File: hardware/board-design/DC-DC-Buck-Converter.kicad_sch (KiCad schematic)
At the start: 18 parts, among them U1 Gate Driver

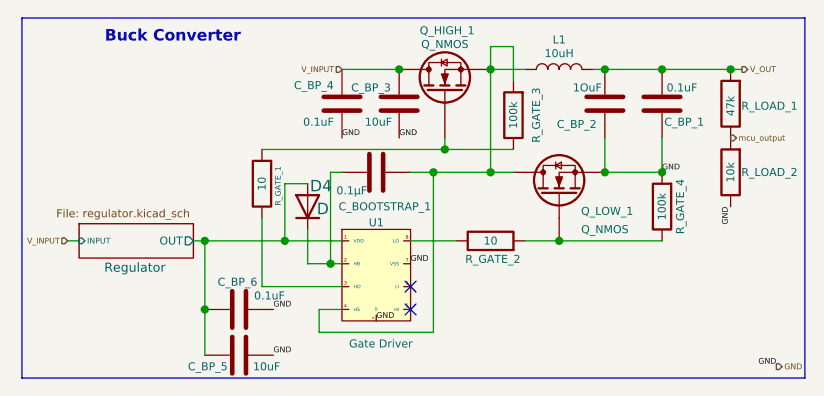
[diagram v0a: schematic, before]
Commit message: feat(schematic): redesign buck converter circuit
Replaced the gate driver and regulator stage with a dedicated Buck Controller IC to resolve missing feedback loops and completed the schematic redesign.
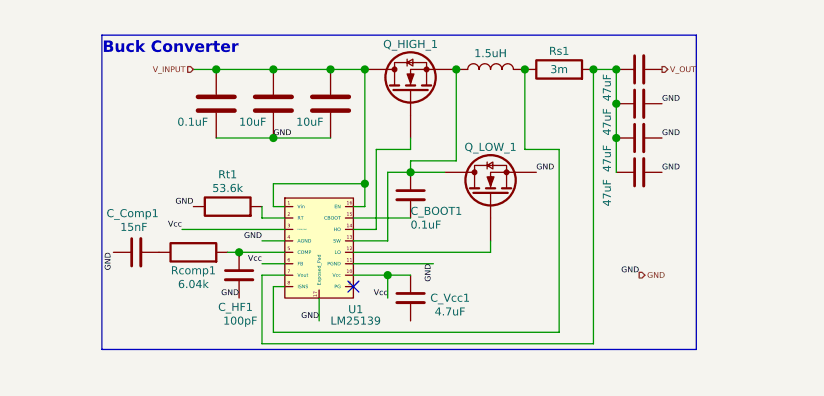
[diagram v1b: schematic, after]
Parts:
- removed C_BOOTSTRAP_1: 0.1µF, Capacitor_SMD:C_0603_1608Metric_Pad1.08x0.95mm_HandSolder, symbol Device:C
- removed C_BP_1, C_BP_6: 0.1uF, Capacitor_SMD:C_0603_1608Metric_Pad1.08x0.95mm_HandSolder, symbol Device:C
- removed C_BP_2: 1OuF, Custom-lib:CAPC6153X390N, symbol Device:C
- removed D4: D, symbol Device:D
- removed R_GATE_1, R_GATE_2: 10, Resistor_SMD:R_0603_1608Metric_Pad0.98x0.95mm_HandSolder, symbol Device:R
- removed R_GATE_3, R_GATE_4: 100k, Resistor_SMD:R_0402_1005Metric_Pad0.72x0.64mm_HandSolder, symbol Device:R
- removed R_LOAD_1: 47k, Resistor_SMD:R_0603_1608Metric_Pad0.98x0.95mm_HandSolder, symbol Device:R
- removed R_LOAD_2: 10k, Resistor_SMD:R_0402_1005Metric_Pad0.72x0.64mm_HandSolder, symbol Device:R
- removed U1: Gate Driver, Custom-lib:SON8 (DRM) (4 mm × 4 mm), symbol Driver_FET:Custom-GateDRVR
- added C_BOOT1: 0.1uF, symbol Device:C_Small
- added C_Comp1: 15nF, symbol Device:C_Small
- added C_HF1: 100pF, symbol Device:C_Small
- added C_Vcc1: 4.7uF, symbol Device:C_Small
- added C_out1, C_out2, C_out3, C_out4: 47uF, symbol Device:C_Small
- added Rcomp1: 6.04k, symbol Device:R
- added Rs1: 3m, symbol Device:R
- added Rt1: 53.6k, symbol Device:R
- added U1: LM25139, Package_DFN_QFN:VQFN-16-1EP_3x3mm_P0.5mm_EP1.68x1.68mm, symbol MySymbols:LM25139
- L1: value 10uH -> 1.5uH
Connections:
- net Regulator/OUT is gone; now on net V_INPUT: C_BP_5.1
- net GND: now also C_Comp1.1, C_HF1.2, C_out1.2, C_out2.2, C_out3.2, Rt1.1, U1.11 (PGND), U1.17 (Exposed_Pad), U1.4 (AGND)
- net V_INPUT: now also U1.1 (Vin), U1.16 (EN)
- net V_OUT: now also C_out4.2; no longer L1.2
- net at L1.1, Q_HIGH_1.S, Q_LOW_1.D: now also C_BOOT1.1, U1.13 (SW)
- net at Q_LOW_1.G: now also U1.12 (LO)
- net at Q_HIGH_1.G: now also U1.14 (HO)
- new net: C_Comp1.2, Rcomp1.1
- new net: C_out1.1, C_out2.1, C_out3.1, C_out4.1, Rs1.2, U1.7 (Vout)
- new net: L1.2, Rs1.1, U1.8 (ISNS)
- new net: C_BOOT1.2, U1.15 (CBOOT)
- new net: Rt1.2, U1.2 (RT)
- new net: C_HF1.1, Rcomp1.2, U1.5 (COMP)
- new net Vcc: C_Vcc1.1, U1.10 (Vcc), U1.3 (FPWM/SYNC), U1.6 (FB)
- no-connect marks 2 -> 1
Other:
- removed sheet Regulator
- moved on the sheet: Q_HIGH_1, Q_LOW_1

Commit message: feat(component-properties): complate properties
Add datasheets, footprints, part numbers and manufacterer names
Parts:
- C_BOOT1: footprint (none) -> Capacitor_SMD:C_0603_1608Metric_Pad1.08x0.95mm_HandSolder; Manufacturer (none) -> Murata Electronics; PART NUMBER (none) -> GRM188R72A104KA35D
- C_BP_3, C_BP_4, C_BP_5: Manufacturer Murata -> Murata Electronics
- C_Comp1: footprint (none) -> Capacitor_SMD:C_0603_1608Metric_Pad1.08x0.95mm_HandSolder; Manufacturer (none) -> Murata Electronics; PART NUMBER (none) -> GCM188R72A153KA37D
- C_HF1: footprint (none) -> Capacitor_SMD:C_0603_1608Metric_Pad1.08x0.95mm_HandSolder; Manufacturer (none) -> Murata Electronics; PART NUMBER (none) -> GRM1885C1H101JA01D
- C_Vcc1: footprint (none) -> Capacitor_SMD:C_0805_2012Metric_Pad1.18x1.45mm_HandSolder; Manufacturer (none) -> Murata Electronics; PART NUMBER (none) -> GRM21BZ71H475KE15L
- C_out1, C_out2, C_out3, C_out4: footprint (none) -> Custom-lib:CAPC6075X690N; Manufacturer (none) -> TDK; PART NUMBER (none) -> CAA573X7S2A476M640LH
- L1: footprint Custom-lib:WE-HCI_2212 -> Custom-lib:WE-LHMI_7030; PART NUMBER 74435581000 -> 74437346015
- Rcomp1: footprint (none) -> Resistor_SMD:R_0603_1608Metric_Pad0.98x0.95mm_HandSolder; Manufacturer (none) -> Vishay; PART NUMBER (none) -> CRCW06036K04FKEA
- Rs1: footprint (none) -> Resistor_SMD:R_0612_1632Metric_Pad1.18x3.40mm_HandSolder; Manufacturer (none) -> Vishay; PART NUMBER (none) -> WSKW06123L000FEA
- Rt1: footprint (none) -> Resistor_SMD:R_0603_1608Metric_Pad0.98x0.95mm_HandSolder; Manufacturer (none) -> Vishay; PART NUMBER (none) -> CRCW060353K6FKEA
- U1: PART NUMBER (none) -> LM25139RGTR; Part Number LM25139RGTR -> (none)
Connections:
- net GND: now also C_Vcc1.2

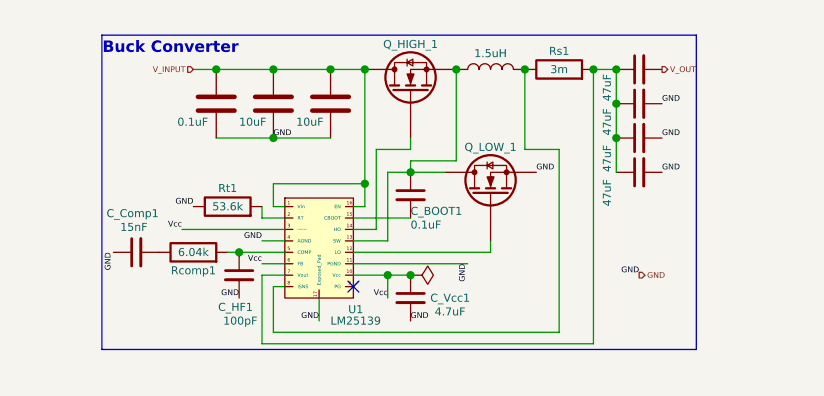
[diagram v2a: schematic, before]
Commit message: feat(schematic): add new symbol and footprint
add for High-MOS and Low-MOS.
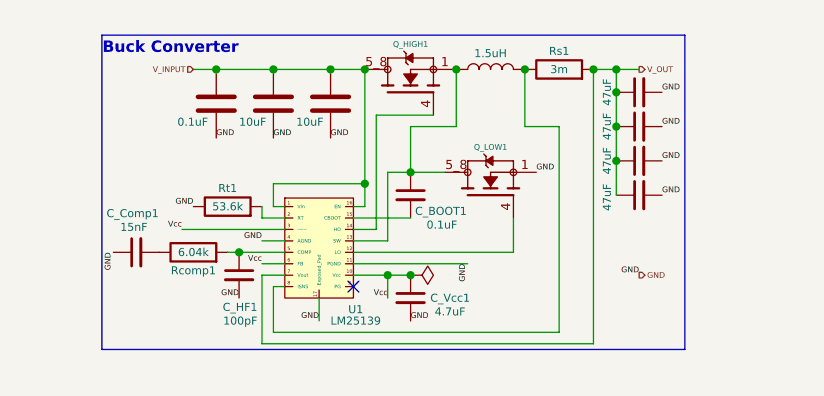
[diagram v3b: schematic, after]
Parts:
- removed Q_HIGH_1, Q_LOW_1: Q_NMOS, Package_SON:VSONP-8-1EP_5x6_P1.27mm, symbol Device:Q_NMOS
- added Q_HIGH1, Q_LOW1: CSD19532Q5B, Custom-lib:TRANS_CSD19532Q5B, symbol MySymbols:CSD19532Q5B
- C_BOOT1, C_BP_3, C_BP_4, C_BP_5, C_Comp1, C_HF1, C_Vcc1: Manufacturer Murata Electronics -> (none)
- C_out1, C_out2, C_out3, C_out4: Manufacturer TDK -> (none)
- L1: Manufacturer Würth Elektronik -> (none)
- Rcomp1, Rs1, Rt1: Manufacturer Vishay -> (none)
- U1: Manufacturer Texas Instruments -> (none); now in the parts list
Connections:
- net GND: now also C_out4.2, Q_LOW1.1, Q_LOW1.2, Q_LOW1.3
- net V_INPUT: now also Q_HIGH1.5_8
- net V_OUT: now also C_out1.1, C_out2.1, C_out3.1, C_out4.1, Rs1.2, U1.7 (Vout); no longer C_out4.2
- net at C_BOOT1.1, L1.1, U1.13 (SW): now also Q_HIGH1.1, Q_HIGH1.2, Q_HIGH1.3, Q_LOW1.5_8
- net at U1.12 (LO): now also Q_LOW1.4
- net at U1.14 (HO): now also Q_HIGH1.4
